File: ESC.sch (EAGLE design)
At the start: 44 parts

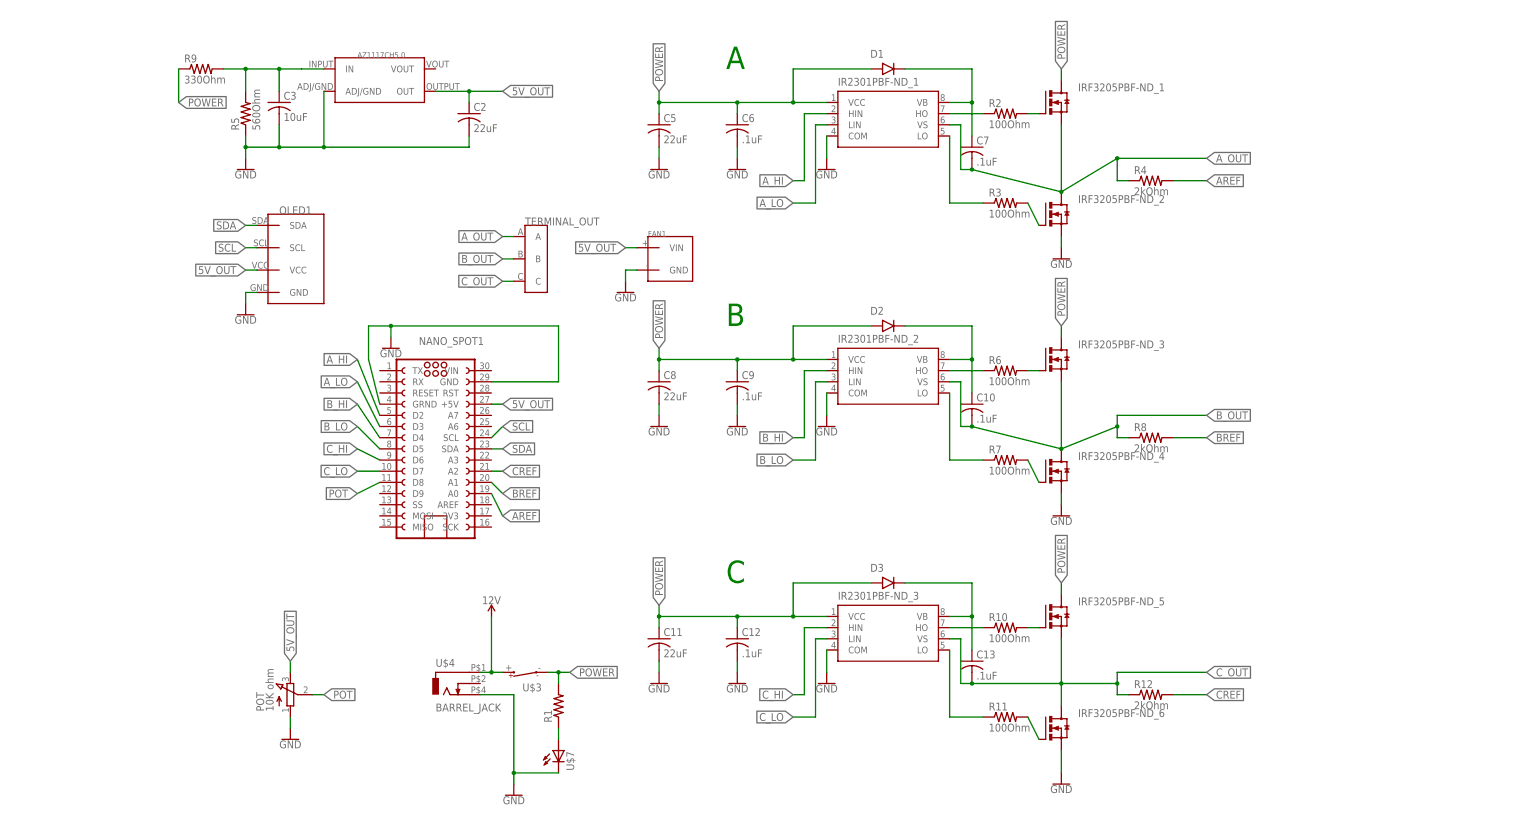
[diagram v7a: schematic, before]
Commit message: parts library and updated schematic
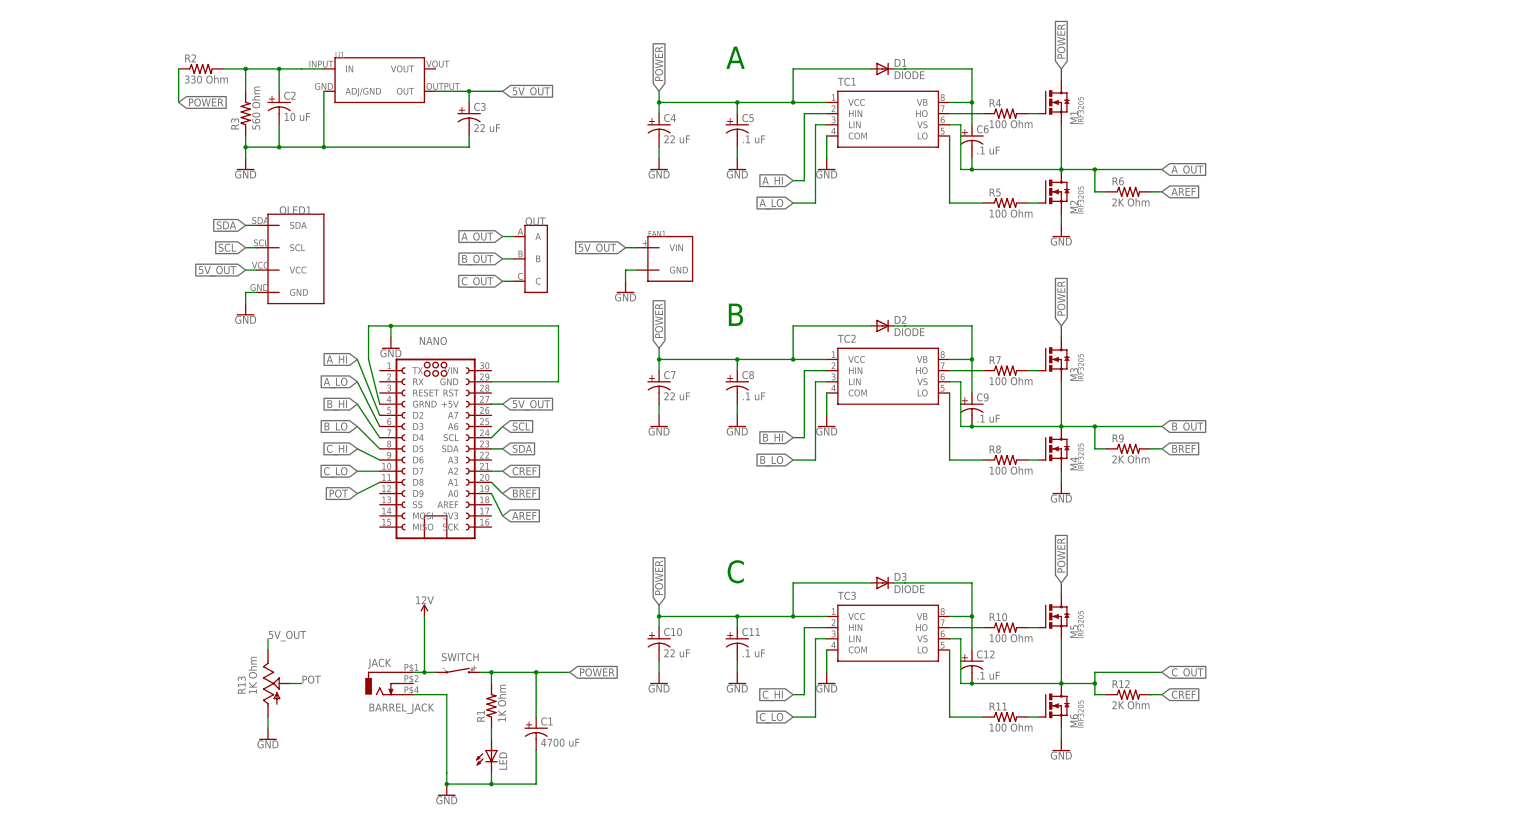
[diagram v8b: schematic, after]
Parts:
- removed C13: .1uF, TRANS_IRF3205SPBF:CAPACITORCERAMIC
- removed IRF3205PBF-ND_2, IRF3205PBF-ND_4, IRF3205PBF-ND_6: (no value), TRANS_IRF3205SPBF:IRF3205
- removed POT: 10K ohm, pot:3RP/1610N
- removed U$3: BOAT_SWITCH, TRANS_IRF3205SPBF:BOAT_SWITCH
- removed U$4: BARREL_JACK, TRANS_IRF3205SPBF:BARREL_JACK
- removed U$7: (no value), TRANS_IRF3205SPBF:LED
- added C1: 4700 uF, TRANS_IRF3205SPBF:CAPACITORLARGE
- added C4: 22 uF, TRANS_IRF3205SPBF:CAPACITORSMALL
- added JACK: BARREL_JACK, TRANS_IRF3205SPBF:BARREL_JACK
- added LED: (no value), TRANS_IRF3205SPBF:LED
- added M2, M4, M6: IRF3205, TRANS_IRF3205SPBF:IRF3205
- added R13: 1K Ohm, TRANS_IRF3205SPBF:POT
- added SWITCH: BOAT_SWITCH, TRANS_IRF3205SPBF:BOAT_SWITCH
- C10, C7: value .1uF -> 22 uF; device TRANS_IRF3205SPBF:CAPACITORCERAMIC -> TRANS_IRF3205SPBF:CAPACITORSMALL
- C11, C5, C8: value 22uF -> .1 uF; device TRANS_IRF3205SPBF:CAPACITORSMALL -> TRANS_IRF3205SPBF:CAPACITORCERAMIC
- C12, C6, C9: value .1uF -> .1 uF
- C2: value 22uF -> 10 uF
- C3: value 10uF -> 22 uF
- D1, D2, D3: value 1N4001 -> DIODE; device 1N4001:1N4001 -> TRANS_IRF3205SPBF:DIODE
- M1, M3, M5: value (none) -> IRF3205
- R1: value (none) -> 1K Ohm
- R10, R11, R7: value 100Ohm -> 100 Ohm
- R12: value 2kOhm -> 2K Ohm
- R2: value 100Ohm -> 330 Ohm
- R3: value 100Ohm -> 560 Ohm
- R4, R8: value 2kOhm -> 100 Ohm
- R5: value 560Ohm -> 100 Ohm
- R6: value 100Ohm -> 2K Ohm
- R9: value 330Ohm -> 2K Ohm
- U1: value AZ1117CH -> (none)
- renumbered AZ1117CH5.0 to U1, IR2301PBF-ND_1 to TC1, IR2301PBF-ND_2 to TC2, IR2301PBF-ND_3 to TC3, IRF3205PBF-ND_1 to M1, IRF3205PBF-ND_3 to M3, IRF3205PBF-ND_5 to M5, NANO_SPOT1 to NANO, TERMINAL_OUT to OUT
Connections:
- removed net N$10: R1.1, U$7.A
- new net N$2: LED.A, R1.1
- net 12V: now also JACK.1, SWITCH.-; no longer U$3.+, U$4.1
- net 5V_OUT: now also C3.ANODE, R13.+; no longer C2.1, POT.E
- net AREF: now also R6.2; no longer R4.2
- net A_OUT: now also C6.CATHODE, M2.D, R6.1; no longer C7.2, IRF3205PBF-ND_2.D, R4.1
- net BREF: now also R9.2; no longer R8.2
- net B_OUT: now also C9.CATHODE, M4.D, R9.1; no longer C10.2, IRF3205PBF-ND_4.D, R8.1
- net C_OUT: now also C12.CATHODE, M6.D; no longer C13.2, IRF3205PBF-ND_6.D
- net GND: now also C1.CATHODE, C10.CATHODE, C11.CATHODE, C2.CATHODE, C3.CATHODE, C4.CATHODE, C5.CATHODE, C7.CATHODE, C8.CATHODE, JACK.3, LED.C, M2.S, M4.S, M6.S, R13.-, R3.1; no longer C11.2, C12.2, C2.2, C3.2, C5.2, C6.2, C8.2, C9.2, IRF3205PBF-ND_2.S, IRF3205PBF-ND_4.S, IRF3205PBF-ND_6.S, POT.A, R5.1, U$4.3, U$7.C
- net N$1: now also M2.G, R5.2; no longer IRF3205PBF-ND_2.G, R3.2
- net N$11: now also C6.ANODE, D1.C; no longer C7.1, D1.CATHODE
- net N$12: now also R7.2; no longer R6.2
- net N$14: now also M4.G, R8.2; no longer IRF3205PBF-ND_4.G, R7.2
- net N$17: now also R7.1; no longer R6.1
- net N$18: now also R8.1; no longer R7.1
- net N$19: now also C9.ANODE, D2.C; no longer C10.1, D2.CATHODE
- net N$24: now also M6.G; no longer IRF3205PBF-ND_6.G
- net N$29: now also C12.ANODE, D3.C; no longer C13.1, D3.CATHODE
- net N$3: now also R4.1; no longer R2.1
- net N$4: now also R4.2; no longer R2.2
- net N$6: now also R5.1; no longer R3.1
- net POT: now also R13.VAR; no longer POT.S
- net POWER: now also C1.ANODE, C10.ANODE, C11.ANODE, C2.ANODE, C4.ANODE, C5.ANODE, C7.ANODE, C8.ANODE, D1.A, D2.A, D3.A, R2.1, R2.2, R3.2, SWITCH.+; no longer C11.1, C12.1, C3.1, C5.1, C6.1, C8.1, C9.1, D1.ANODE, D2.ANODE, D3.ANODE, R5.2, R9.1, R9.2, U$3.-
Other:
- moved on the sheet: R1, R12, R2, R3, R4, R5, R6, R7, R8, R9
